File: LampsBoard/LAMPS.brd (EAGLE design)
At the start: 102.2 x 53.3 mm, 65 parts, among them IC1 UA741P, IC3 5V, IC4 78L12Z, IC5 78L12Z, IC6 UA741P, Q1 TIP120

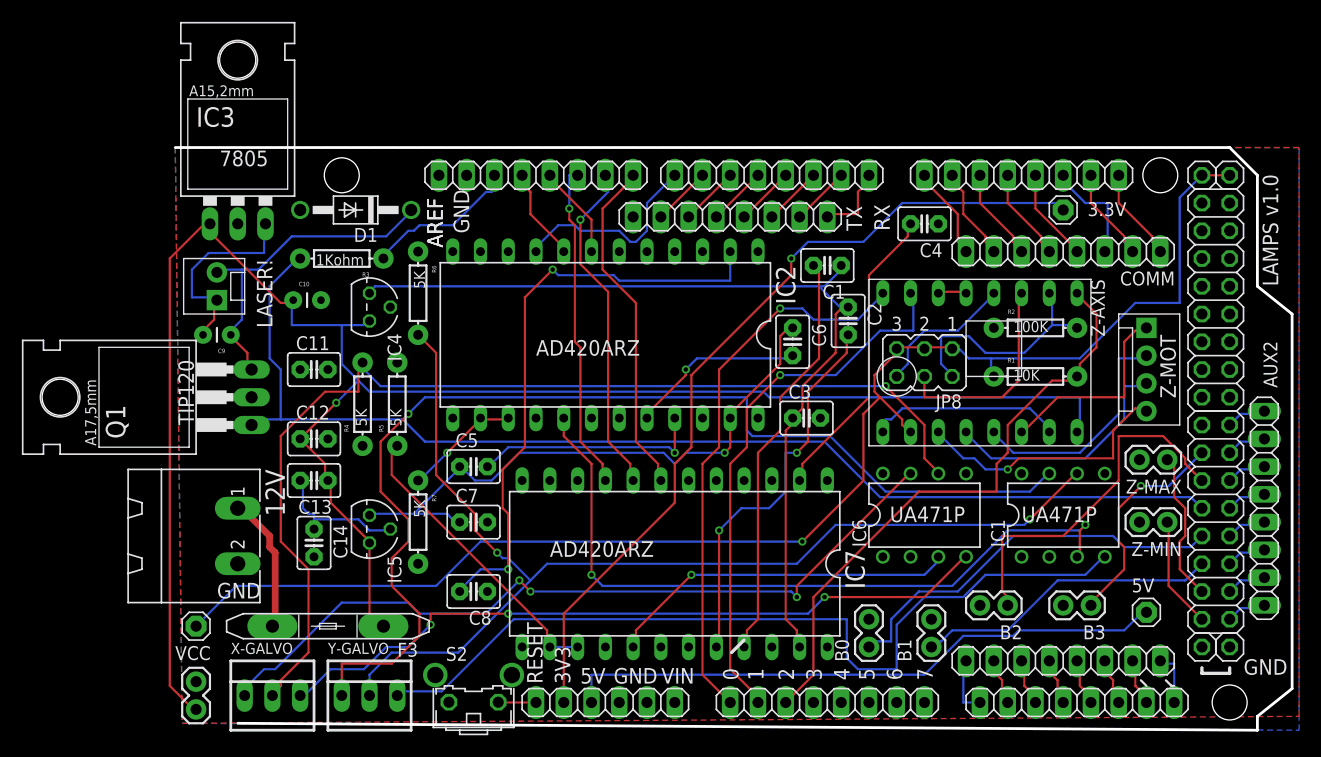
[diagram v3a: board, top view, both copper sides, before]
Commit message: Remove expensive component for DIY variety
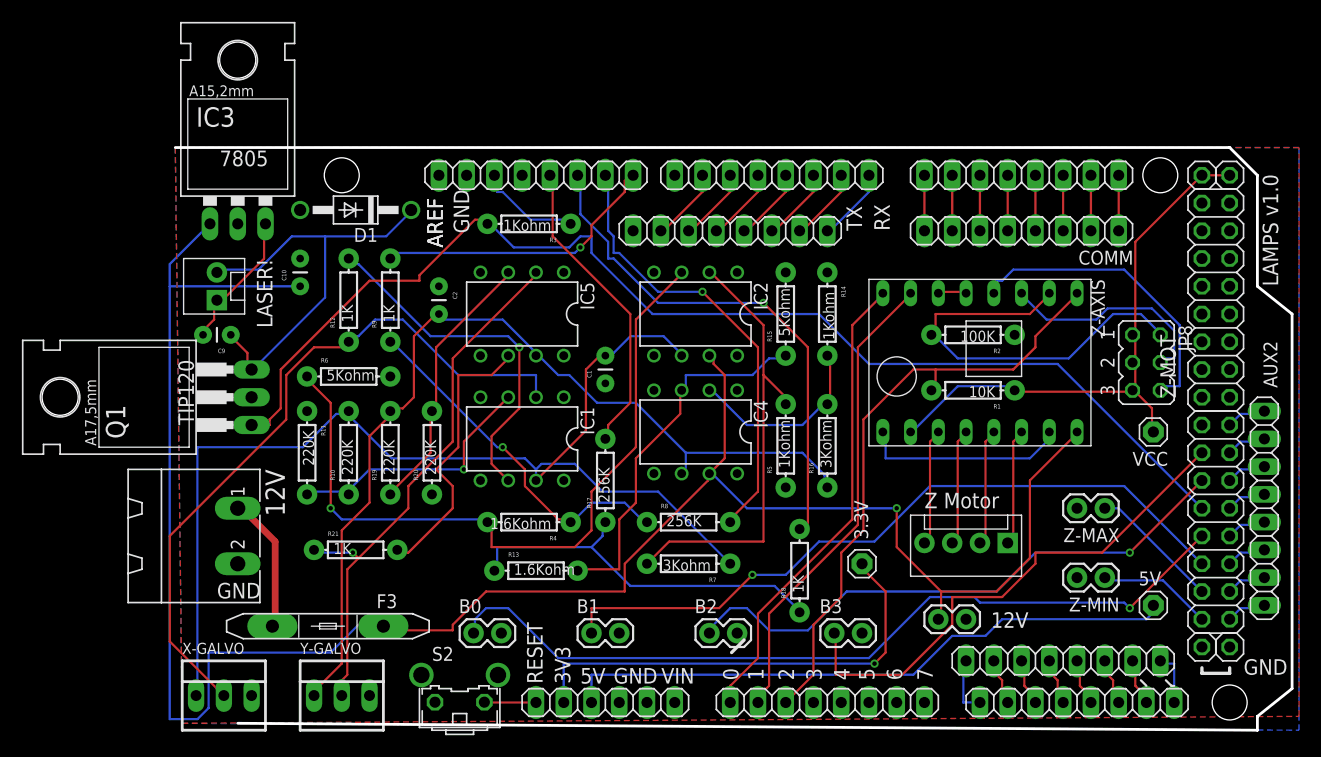
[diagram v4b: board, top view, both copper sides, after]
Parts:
- removed C11: 10nF, capacitor-wima:C2.5-3
- removed C12, C13: 330 nF, capacitor-wima:C2.5-3
- removed C14, C5, C6: 10 nF, capacitor-wima:C2.5-3
- removed C3, C4, C7, C8: 100 nF, capacitor-wima:C2.5-3
- removed IC6: UA741P, linear:DIL08
- removed IC7: (no value), ic-package:DIL24-6
- added R10, R11, R19, R20: 220K, SparkFun:AXIAL-0.3
- added R12, R18, R21, R9: 1K, SparkFun:AXIAL-0.3
- added R13: 1.6Kohm, SparkFun:AXIAL-0.3
- added R14: 1Kohm, SparkFun:AXIAL-0.3
- added R15: 5Kohm, SparkFun:AXIAL-0.3
- added R16: 3Kohm, SparkFun:AXIAL-0.3
- added R17, R8: 256K, SparkFun:AXIAL-0.3
- C1, C2: value 10 nF -> 220uF; device capacitor-wima:C2.5-3 -> SparkFun:CAP-PTH-SMALL
- IC1: value UA741P -> LM741P
- IC2: value (none) -> LM741P; device ic-package:DIL24-6 -> linear:DIL08
- IC4, IC5: value 78L12Z -> LM741P; device linear:TO92 -> linear:DIL08
- R4: value 5K -> 1.6Kohm
- R5: value 5K -> 1Kohm
- R6: value 5K -> 5Kohm
- R7: value 5K -> 3Kohm
- moved VCC 89.4 mm to (89.5, 27.3)
- moved 12V-AUX 68.4 mm to (69.8, 10.2), turned to 0 degrees
- moved IC1 50.0 mm to (31.8, 26.7), turned to 180 degrees
- moved C2 37.6 mm to (24.1, 40.6)
- moved 3.3V 37.3 mm to (62.9, 15.2), turned to 270 degrees
- moved B0 36.2 mm to (27.3, 8.89), turned to 0 degrees
- moved R5 35.8 mm to (55.9, 26.0)
- moved IC4 32.0 mm to (47.6, 27.3), turned to 180 degrees
- moved B1 31.1 mm to (38.1, 8.89), turned to 0 degrees
- moved B2 27.4 mm to (48.9, 8.89), turned to 0 degrees
- moved R7 25.1 mm to (47.0, 15.2), turned to 180 degrees
- moved IC5 24.1 mm to (31.8, 38.1), turned to 180 degrees
- moved B3 23.6 mm to (60.3, 8.89), turned to 0 degrees
- moved Z-MOT 23.4 mm to (76.2, 17.1), turned to 180 degrees
- moved C1 23.0 mm to (39.4, 31.8), turned to 90 degrees
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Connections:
- removed net N$30: IC2.14, IC2.15, R7.P$1
- removed net N$31: IC1.6, R6.P$2, Y-GALVO.2
- removed net N$32: IC1.4, Y-GALVO.3
- removed net N$33: IC1.7, Y-GALVO.1
- removed net N$34: IC1.3, IC2.17
- net +12V: now also IC2.7, IC4.7; no longer C12.1, C13.1, IC4.3, IC5.3
- net D10: now also R18.P$2; no longer IC7.9
- net D11: now also R17.P$2; no longer IC2.7
- net D12: no longer IC2.8
- net D7: no longer IC2.9
- net D8: now also R9.P$2; no longer IC7.7
- net D9: now also R8.P$2; no longer IC7.8
- net GND: now also C1.1, C2.1, IC1.4, IC4.4, IC5.4, R11.P$1, R14.P$1, R15.P$2, R20.P$1, R5.P$1, R6.P$2, X-GALVO.3, Y-GALVO.3; no longer C11.1, C11.2, C12.2, C14.2, C3.2, C4.1, C7.2, C8.1, IC1.2, IC2.11, IC2.5, IC2.6, IC4.2, IC6.2, IC7.11, IC7.4, IC7.5, IC7.6, R4.P$1, R5.P$2, R6.P$1, R7.P$2
- net N$1: now also IC2.3, R4.P$2, R6.P$1; no longer C5.2, IC2.21
- net N$18: now also IC1.2, R12.P$1, X-GALVO.2; no longer C1.1, C2.1, C3.1, IC4.1, IC7.23
- net N$19: now also IC4.2, R14.P$2, R16.P$2; no longer C4.2, IC7.2
- net N$2: now also IC2.2, R5.P$2, R7.P$2; no longer C6.2, IC2.20
- net N$24: now also R13.P$1, R17.P$1, R18.P$1; no longer C8.2, IC2.2
- net N$25: now also C2.2, IC4.6, IC5.7, R16.P$1, R19.P$2, Y-GALVO.1; no longer C5.1, C6.1, C7.1, IC2.23, IC5.1
- net N$26: now also IC5.3, R19.P$1, R20.P$2; no longer C13.2, C14.1, IC5.2
- net N$27: now also IC5.6, R21.P$2; no longer IC6.4, X-GALVO.3
- net N$28: now also IC5.2, R21.P$1, Y-GALVO.2; no longer IC6.7, X-GALVO.1
- net N$3: now also IC1.3, R10.P$1, R11.P$2; no longer C1.2, IC7.21
- net N$4: now also R4.P$1, R8.P$1, R9.P$1; no longer C2.2, IC7.20
- net N$5: now also IC4.3, R13.P$2, R15.P$1; no longer IC6.3, IC7.17
- net N$6: now also C1.2, IC1.7, IC2.6, R10.P$2, R7.P$1, X-GALVO.1; no longer IC7.14, IC7.15, R5.P$1
- net N$7: now also IC1.6, R12.P$2; no longer IC6.6, R4.P$2, X-GALVO.2
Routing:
- net N$31: track 101.3 -> 0.00 mm, vias 2 -> 0
- net N$33: track 100.5 -> 0.00 mm, vias 1 -> 0
- net N$32: track 78.5 -> 0.00 mm
- net VCC: track 130.6 -> 52.3 mm, vias 1 -> 0
- net N$6: track 27.3 -> 103.3 mm
- net N$34: track 66.6 -> 0.00 mm, vias 2 -> 0
- net N$7: track 97.4 -> 33.1 mm
- net N$1: track 21.2 -> 67.1 mm
- net N$27: track 66.8 -> 26.1 mm, vias 3 -> 0
- net D46: track 36.7 -> 75.6 mm, vias 0 -> 1
- net D48: track 28.2 -> 65.7 mm, vias 0 -> 1
- net N$8: track 76.6 -> 42.5 mm
- net N$25: track 55.9 -> 86.0 mm, vias 1 -> 0
- net D40: track 20.1 -> 47.9 mm, vias 1 -> 0
- net N$2: track 16.3 -> 41.8 mm, vias 1 -> 0
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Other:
- board text added: "12V"
- board text added: "Z Motor"
- board text removed: "AD420ARZ"
- board text removed: "UA471P"
